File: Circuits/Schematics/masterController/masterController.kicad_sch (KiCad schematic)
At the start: 35 parts, among them J1 Conn_01x05_Pin, J2 Conn_02x03_Counter_Clockwise, K1 Relay_SPDT, SW1 SW_Push, SW2 SW_Push_Open, U1 LM2596S-ADJ, U2 AMS1117-3.3, U3 STM32F411CEUx, U4 MAX485E

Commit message: PCB Updates
Şematikler temize çekildi.
motorDriverAtmega hatalı RS-485 DE (pin 3) bağlantısı düzeltildi.
masterController şematiği tamamlandı.
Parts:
- removed R7: R, symbol Device:R
- added F2: 5A, symbol Device:Fuse
- added R6: 1k / 1W, symbol Device:R
- renumbered C10 to C1, C6 to C10, C16 to C11, C13 to C12, C15 to C13, C8 to C14, C7 to C15, C9 to C16, C1 to C2, C2 to C3, C3 to C4, C11 to C5, C14 to C6, C4 to C7, C12 to C8, C5 to C9, F2 to F1, J2 to J1, J1 to J2, R6 to R3, R3 to R4, R4 to R5, R5 to R7, U3 to U1, U1 to U2, U2 to U3
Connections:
- net GND: now also K1.A2, R6.2; no longer K1.12, K1.A1, SW2.1 (A)
- net VDD: now also F2.1
- net at SW2.2 (B): now also F2.2; no longer K1.A2
- new net: K1.A1, SW2.1 (A)
- new net: K1.12, R6.1
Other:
- note added: "24V+ 14A+"
- note added: "Fuse: Amper değerinin 2.5 katı seçilecek"
- note removed: "WIP"
- moved on the sheet: C1, C12, C14, C16, C5, C8, D1, F1, J1, J2, K1, L1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

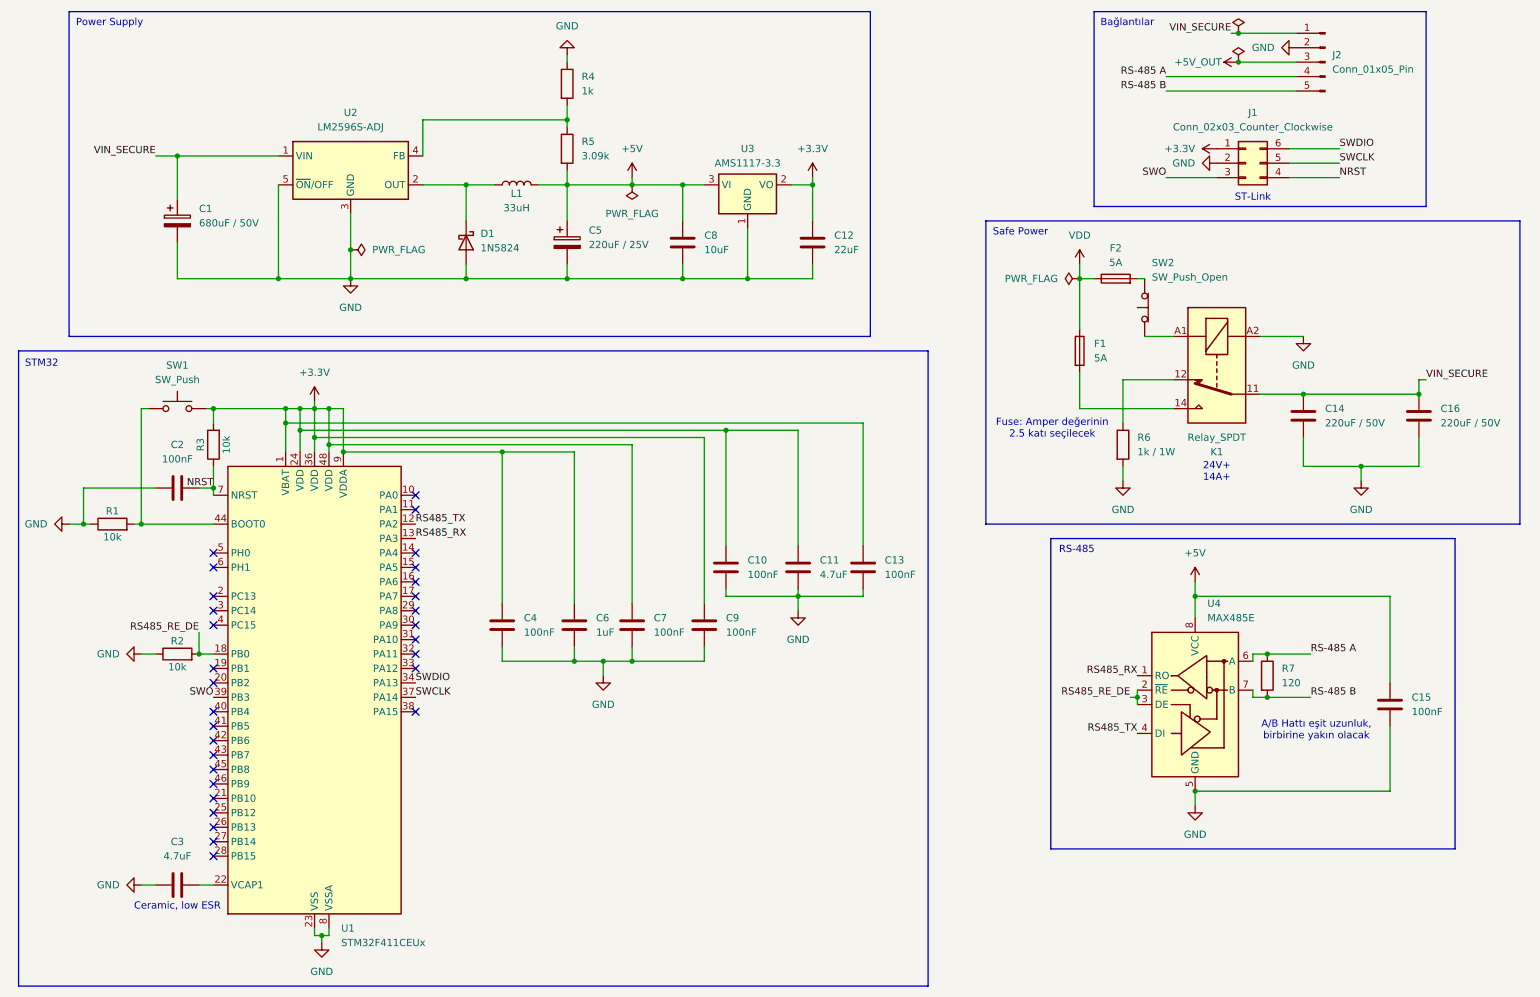
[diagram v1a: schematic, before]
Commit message: Bug fixes, footprint assignments
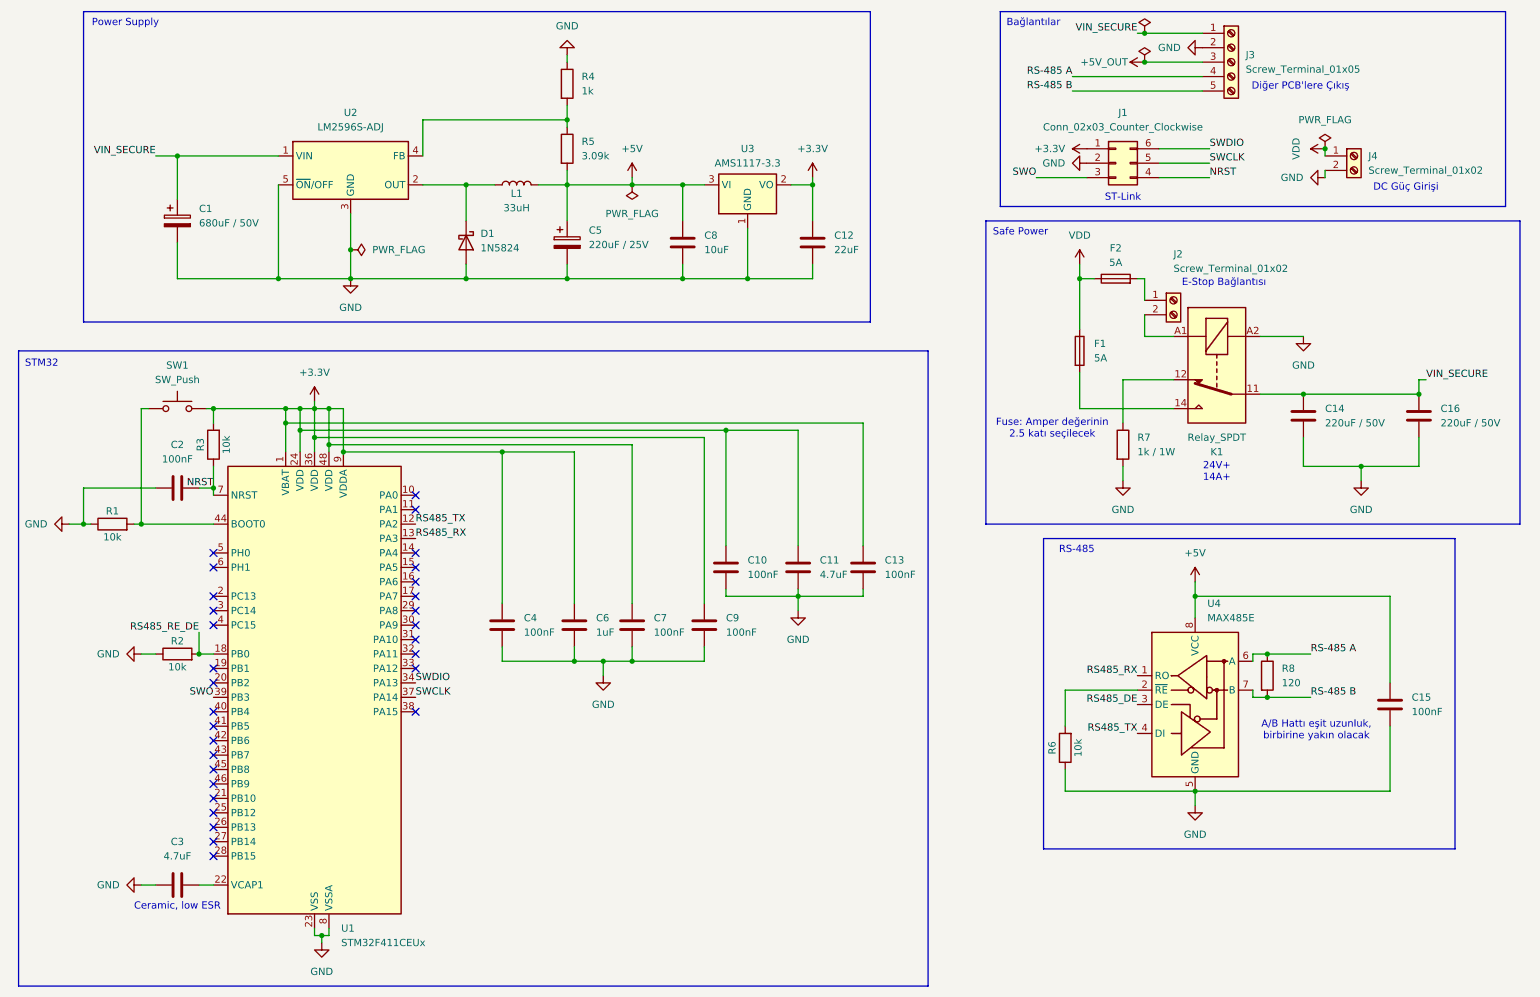
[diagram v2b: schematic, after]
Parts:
- removed J2: Conn_01x05_Pin, symbol Connector:Conn_01x05_Pin
- removed SW2: SW_Push_Open, symbol Switch:SW_Push_Open
- added J2, J4: Screw_Terminal_01x02, TerminalBlock_Phoenix:TerminalBlock_Phoenix_PT-1,5-2-5.0-H_1x02_P5.00mm_Horizontal, symbol Connector:Screw_Terminal_01x02
- added J3: Screw_Terminal_01x05, TerminalBlock_Phoenix:TerminalBlock_Phoenix_PT-1,5-5-5.0-H_1x05_P5.00mm_Horizontal, symbol Connector:Screw_Terminal_01x05
- added R6: 10k, Resistor_SMD:R_0805_2012Metric_Pad1.20x1.40mm_HandSolder, symbol Device:R
- C1: footprint (none) -> Capacitor_THT:C_Radial_D12.5mm_H25.0mm_P5.00mm
- C10, C13, C15, C2, C4, C6, C7, C9: footprint (none) -> Capacitor_SMD:C_0805_2012Metric_Pad1.18x1.45mm_HandSolder
- C11, C3: footprint (none) -> Capacitor_SMD:C_Elec_5x5.4
- C12: footprint (none) -> Capacitor_SMD:C_Elec_6.3x5.4
- C14, C16, C5: footprint (none) -> Capacitor_SMD:C_Elec_10x10.2
- C8: footprint (none) -> Capacitor_SMD:C_Elec_6.3x5.8
- D1: footprint (none) -> Diode_SMD:D_SMC_Handsoldering
- F1, F2: footprint (none) -> Fuse:Fuseholder_Cylinder-5x20mm_Schurter_0031_8201_Horizontal_Open
- J1: footprint (none) -> Connector_PinHeader_2.54mm:PinHeader_2x03_P2.54mm_Vertical
- K1: footprint (none) -> Relay_THT:Relay_SPDT_Finder_40.61
- L1: footprint (none) -> Inductor_SMD:L_12x12mm_H8mm
- R1, R2, R3, R4, R5: footprint (none) -> Resistor_SMD:R_0805_2012Metric_Pad1.20x1.40mm_HandSolder
- R7: renamed from R6; footprint (none) -> Resistor_SMD:R_2512_6332Metric
- R8: renamed from R7; footprint (none) -> Resistor_SMD:R_0805_2012Metric_Pad1.20x1.40mm_HandSolder
- SW1: footprint (none) -> Button_Switch_THT:SW_PUSH_6mm_H4.3mm
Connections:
- net +5V_OUT: now also J3.3 (Pin_3)
- net GND: now also J3.2 (Pin_2), J4.2 (Pin_2), R6.1
- net RS-485 A: now also J3.4 (Pin_4)
- net RS-485 B: now also J3.5 (Pin_5)
- net RS485_RE_DE: no longer U4.2 (~{RE}), U4.3 (DE)
- net VDD: now also J4.1 (Pin_1)
- net VIN_SECURE: now also J3.1 (Pin_1)
- net at K1.A1: now also J2.2 (Pin_2)
- net at F2.2: now also J2.1 (Pin_1)
- new net: R6.2, U4.2 (~{RE})
- new net RS485_DE: U4.3 (DE)
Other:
- note added: "DC Güç Girişi"
- note added: "Diğer PCB'lere Çıkış"
- note added: "E-Stop Bağlantısı"
- moved on the sheet: J1

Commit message: Main Controller PCB Completed
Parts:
- removed J3: Screw_Terminal_01x05, TerminalBlock_Phoenix:TerminalBlock_Phoenix_PT-1,5-5-5.0-H_1x05_P5.00mm_Horizontal, symbol Connector:Screw_Terminal_01x05
- added J5: Screw_Terminal_01x02, TerminalBlock_Phoenix:TerminalBlock_Phoenix_PT-1,5-2-5.0-H_1x02_P5.00mm_Horizontal, symbol Connector:Screw_Terminal_01x02
- added J6: Screw_Terminal_01x03, TerminalBlock_Phoenix:TerminalBlock_Phoenix_PT-1,5-3-5.0-H_1x03_P5.00mm_Horizontal, symbol Connector:Screw_Terminal_01x03
- C14, C16: footprint Capacitor_SMD:C_Elec_10x10.2 -> Capacitor_THT:CP_Radial_D10.0mm_P5.00mm
- F1, F2: value 5A -> 35A; footprint Fuse:Fuseholder_Cylinder-5x20mm_Schurter_0031_8201_Horizontal_Open -> LebowskiBotCustomLibrary:HT-01-A
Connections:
- net +5V: now also J6.1 (Pin_1)
- net GND: now also J5.1 (Pin_1); no longer C10.1, C11.1, C12.2, C13.1, C15.2, C2.1, C3.1, C4.1, C6.1, C7.1, C8.2, C9.1, J1.2 (Pin_2), R1.1, R2.1, R4.1, R6.1, U1.23 (VSS), U1.35 (VSS), U1.47 (VSS), U1.49 (VSS), U1.8 (VSSA), U3.1 (GND), U4.5 (GND)
- net RS-485 A: now also J6.3 (Pin_3)
- net RS-485 B: now also J6.2 (Pin_2)
- net RS485_DE: now also U1.10 (PA0)
- net SWCLK: now also J1.6 (Pin_6); no longer J1.5 (Pin_5)
- net SWDIO: now also J1.5 (Pin_5); no longer J1.6 (Pin_6)
- net VIN_SECURE: now also J5.2 (Pin_2)
- new net GNDL: C10.1, C11.1, C12.2, C13.1, C15.2, C2.1, C3.1, C4.1, C6.1, C7.1, C8.2, C9.1, J1.2 (Pin_2), R1.1, R2.1, R4.1, R6.1, U1.23 (VSS), U1.35 (VSS), U1.47 (VSS), U1.49 (VSS), U1.8 (VSSA), U3.1 (GND), U4.5 (GND)
- no-connect marks 30 -> 29
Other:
- note added: "Diğer PCB'lere Logic"
